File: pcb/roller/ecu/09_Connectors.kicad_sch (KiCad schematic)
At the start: 1 part, among them J5 6437288-3

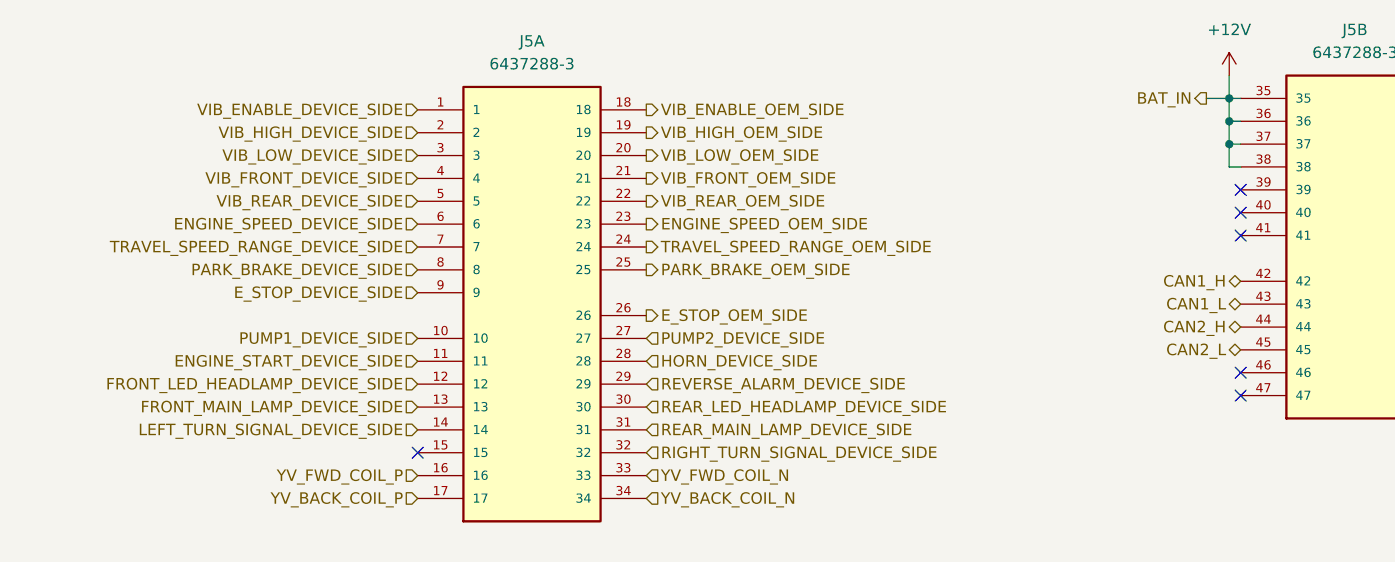
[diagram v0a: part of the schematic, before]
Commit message: Add design settings and DRC rules to ECU PCB configuration
- Introduced comprehensive design settings including defaults for various parameters such as line widths, text sizes, and pad dimensions.
- Added detailed DRC (Design Rule Check) exclusions and rule severities to enhance error handling and warnings during PCB design.
- Updated tuning pattern settings and teardrop parameters for improved track and pad connections.
- Cleared previously used designators for better organization and clarity in the design file.
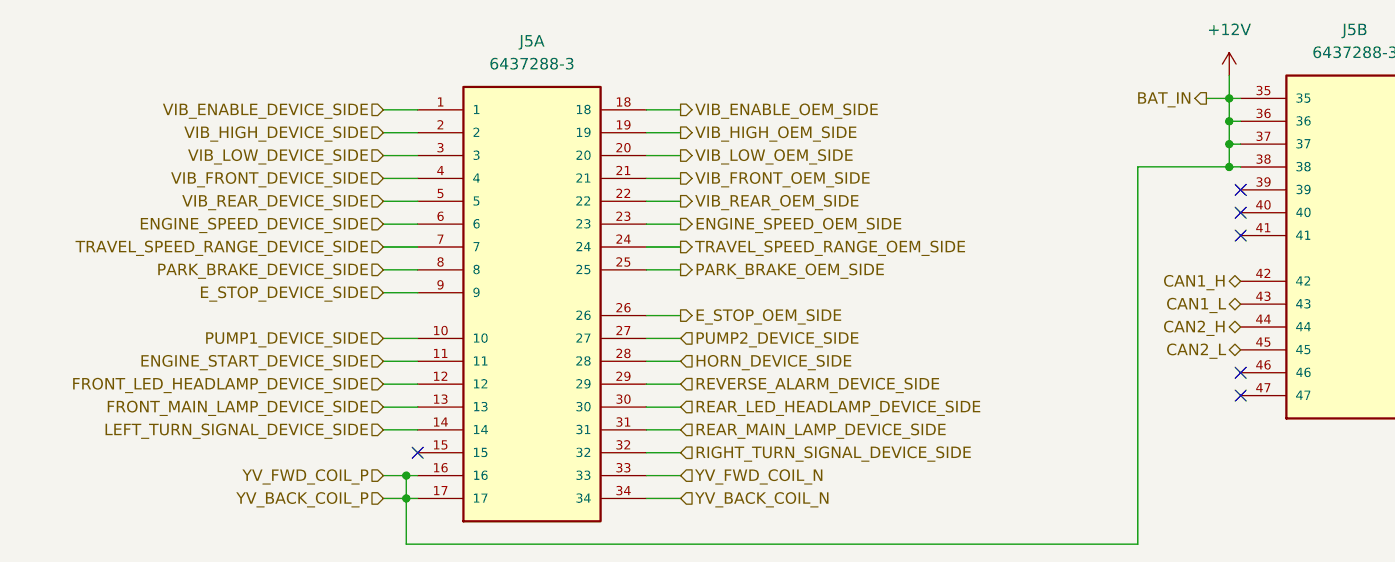
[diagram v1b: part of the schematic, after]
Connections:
- net YV_BACK_COIL_P is gone; now on net +12V: J5.17
- net YV_FWD_COIL_P is gone; now on net +12V: J5.16

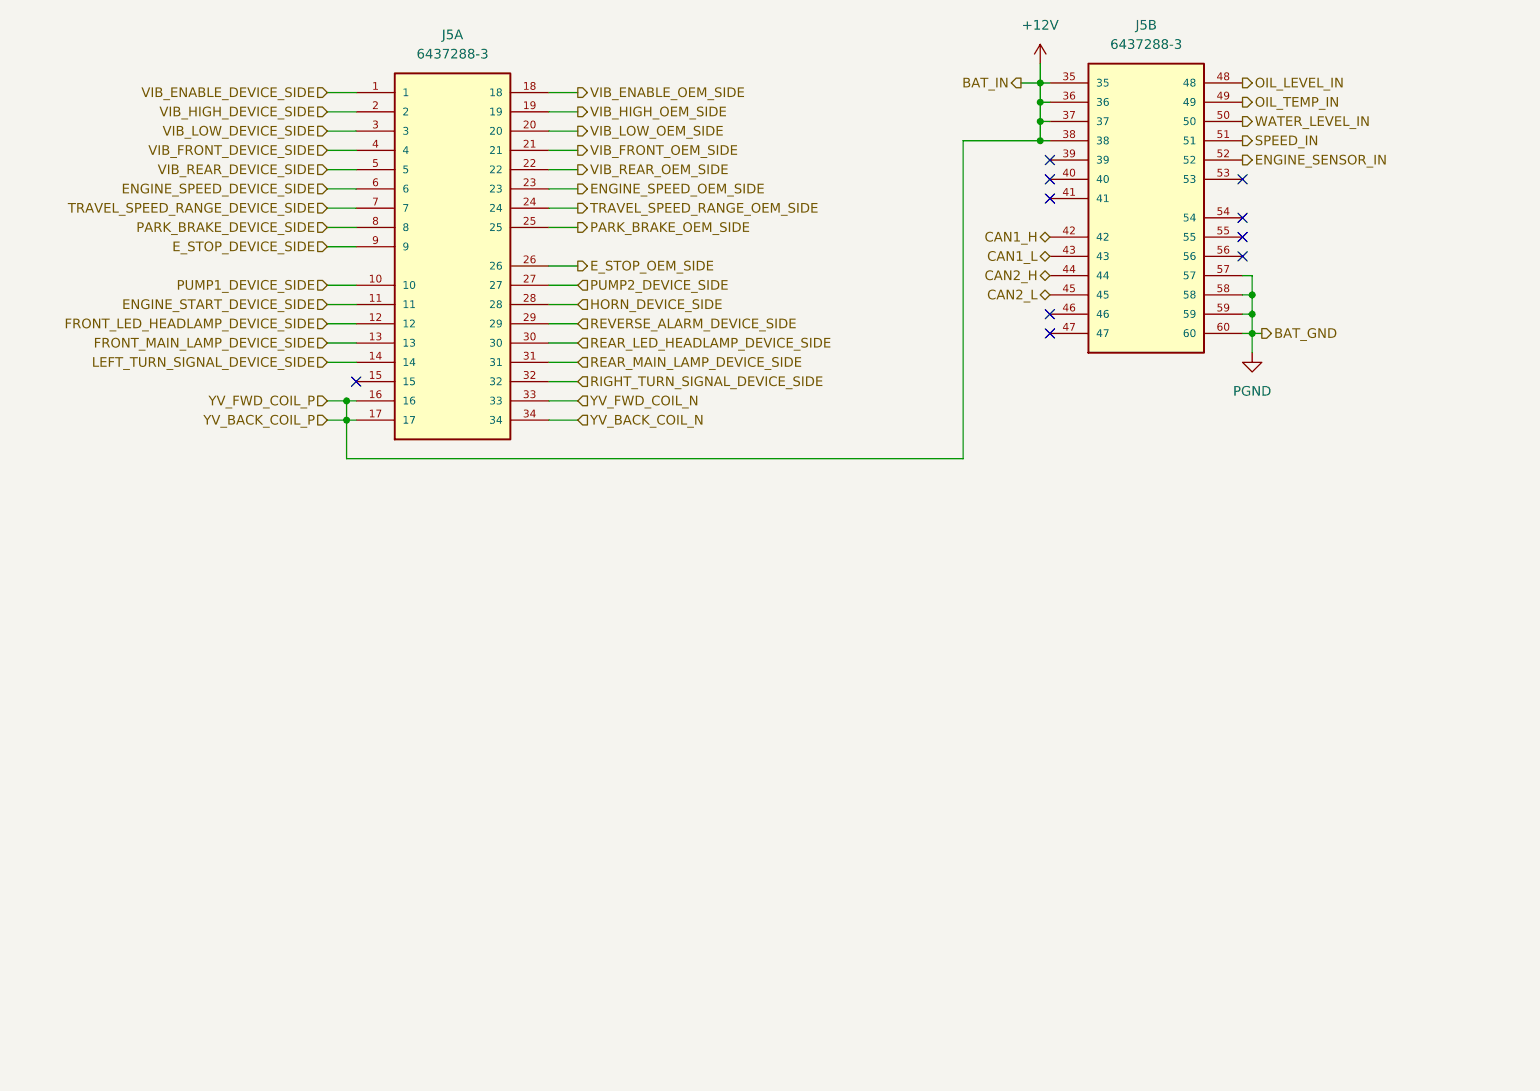
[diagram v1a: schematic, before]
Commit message: Add ESTOP_NC pin and wire connections in ECU schematic; update designators in PCB project
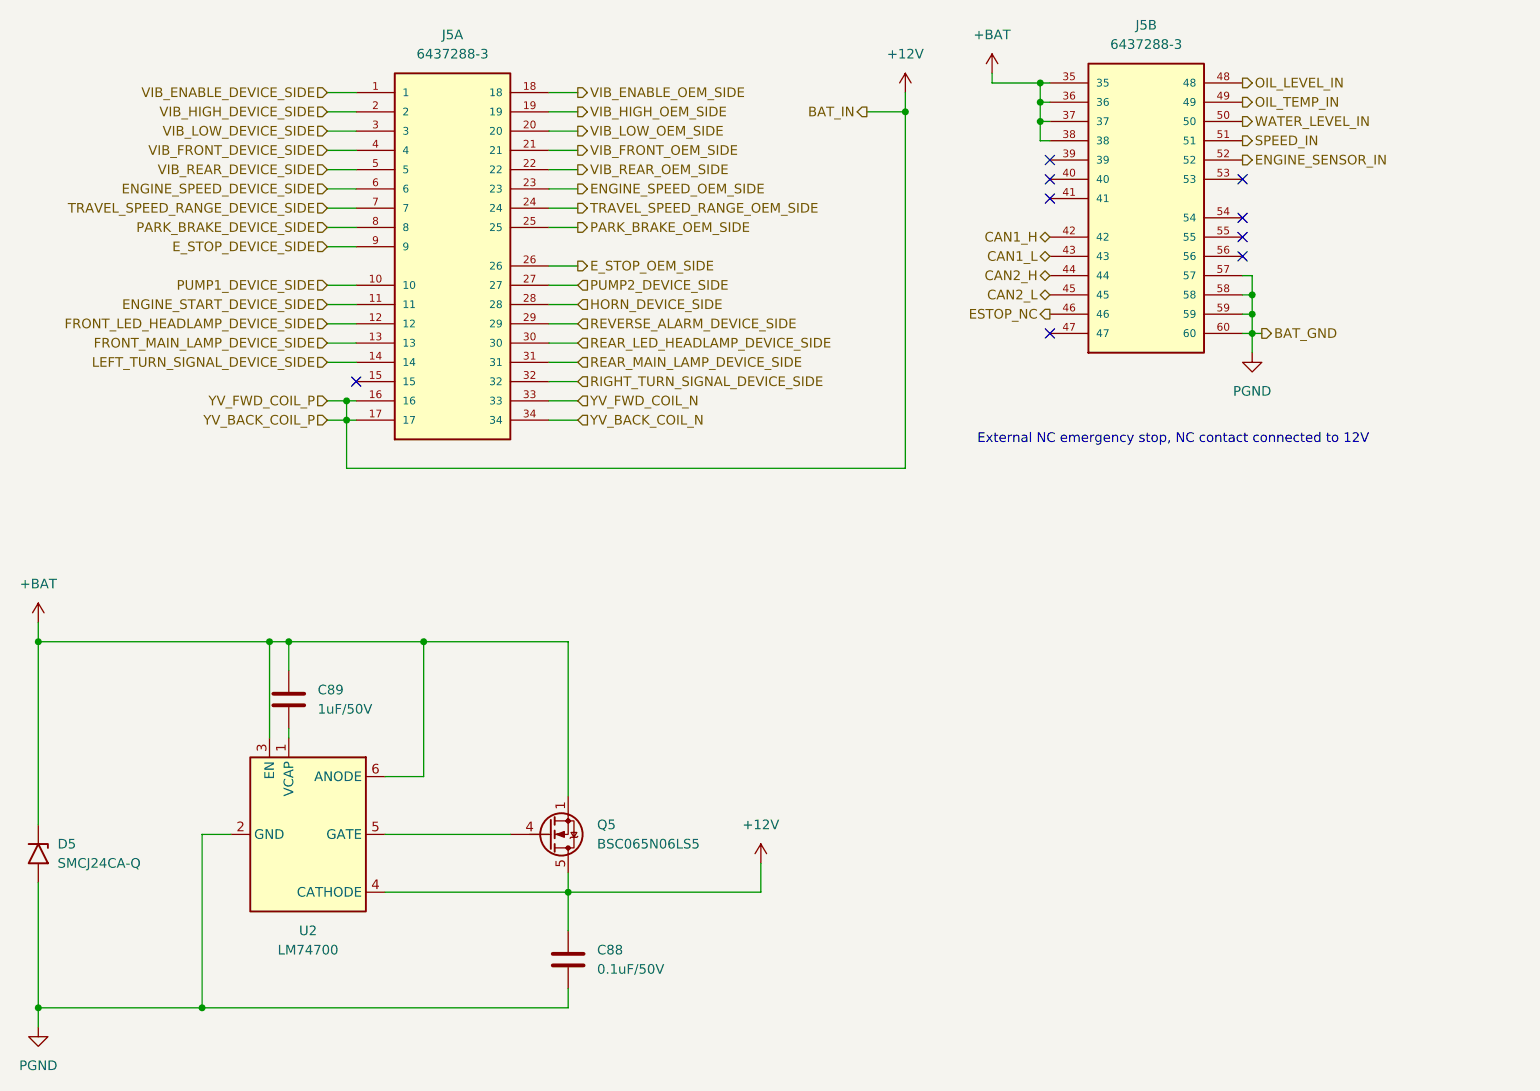
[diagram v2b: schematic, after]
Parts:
- added C88: 0.1uF/50V, Capacitor_SMD:C_0603_1608Metric, symbol Device:C
- added C89: 1uF/50V, Capacitor_SMD:C_0603_1608Metric, symbol Device:C
- added D5: SMCJ24CA-Q, Diode_SMD:D_SMC, symbol Diode:1.5SMCxxA
- added Q5: BSC065N06LS5, Package_TO_SOT_SMD:TDSON-8-1, symbol Transistor_FET:BSC060N10NS3G
- added U2: LM74700, Package_TO_SOT_SMD:SOT-23-6, symbol Power_Management:LM74700
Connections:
- net +12V: now also C88.1, Q5.5 (D), U2.4 (CATHODE); no longer J5.35, J5.36, J5.37, J5.38
- net PGND: now also C88.2, D5.2 (A2), U2.2 (GND)
- net ESTOP_NC: now reaches J5.46
- new net: C89.2, U2.1 (VCAP)
- new net: Q5.4 (G), U2.5 (GATE)
- new net +BAT: C89.1, D5.1 (A1), J5.35, J5.36, J5.37, J5.38, Q5.1 (S), Q5.2 (S), Q5.3 (S), U2.3 (EN), U2.6 (ANODE)
- no-connect marks 10 -> 9
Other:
- note added: "External NC emergency stop, NC contact connected to 12V"

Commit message: Refactor ECU schematic and project files
- Updated used designators in ecu.kicad_pro to reflect current components.
- Adjusted wire connections in ecu.kicad_sch for better layout and clarity.
- Added new wires and labels for ESTOP functionality.
- Modified pin placements and sizes for improved organization in the schematic.
- Ensured all changes maintain compatibility with existing design specifications.
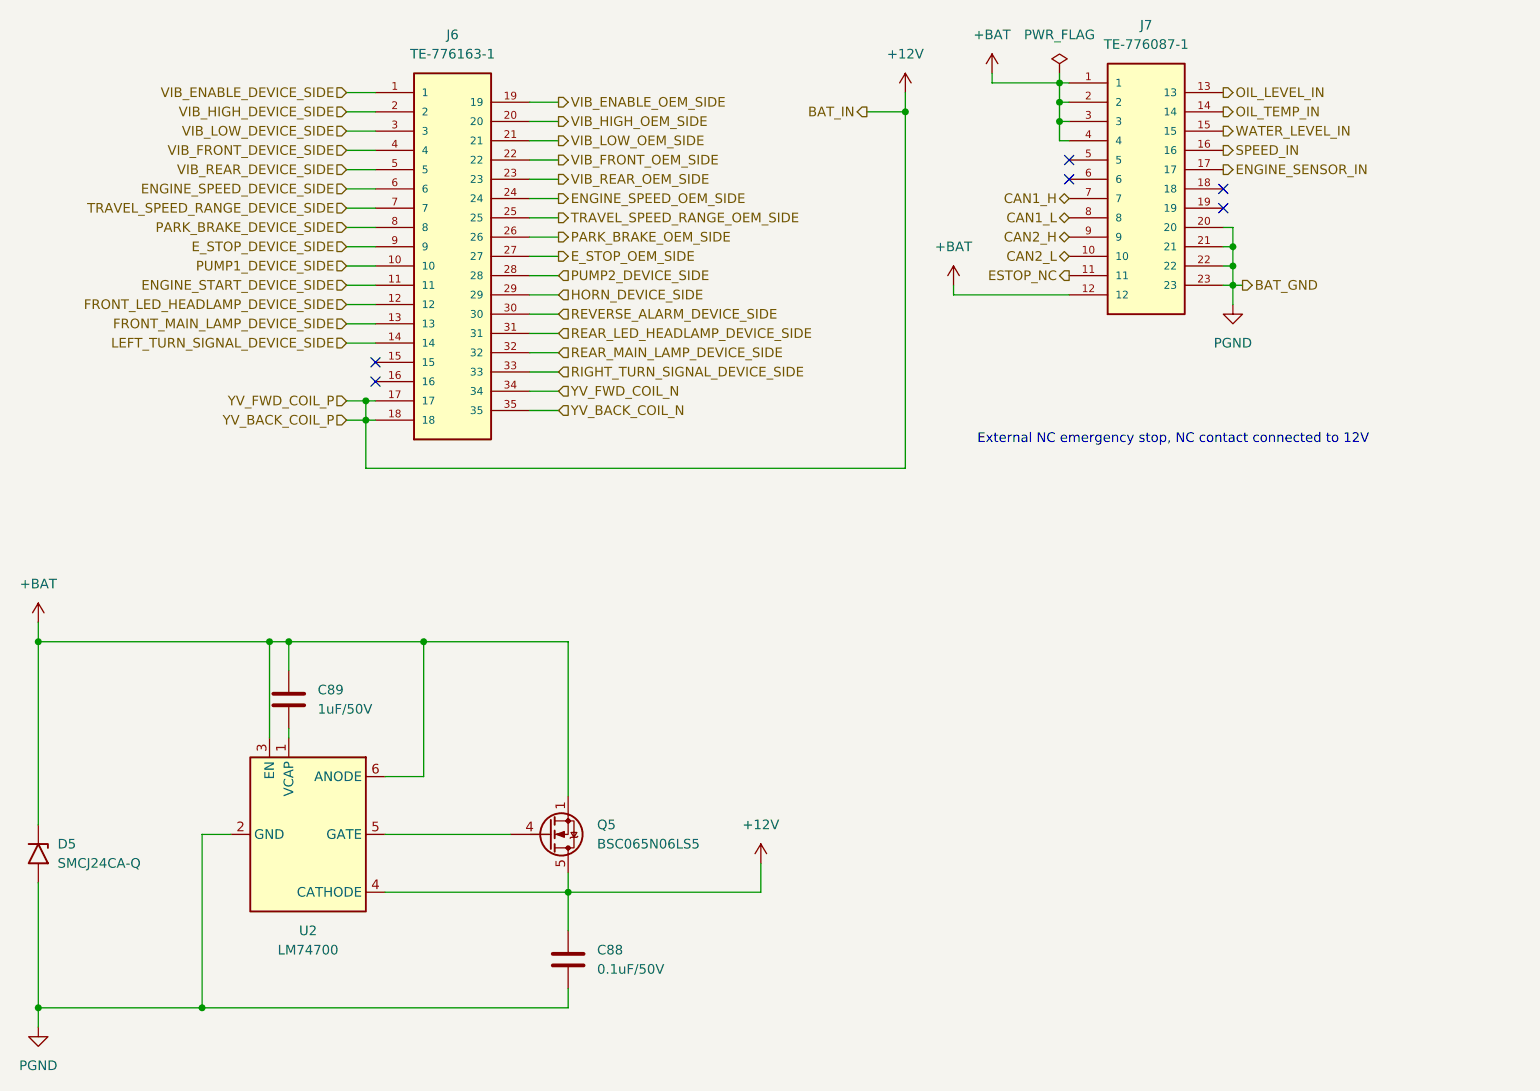
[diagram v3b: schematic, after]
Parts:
- removed J5: 6437288-3, Starlight:TE_6437288-3, symbol Starlight:6437288-3
- added J6: TE-776163-1, Starlight:TE_776163-1, symbol Starlight:TE-776163-1
- added J7: TE-776087-1, Starlight:TE_776087-1, symbol Starlight:TE-776087-1
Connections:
- net +12V: now also J6.17, J6.18
- net +BAT: now also J7.1, J7.12, J7.2, J7.3, J7.4
- net CAN1_H: now also J7.7
- net CAN1_L: now also J7.8
- net CAN2_H: now also J7.9
- net CAN2_L: now also J7.10
- net ENGINE_SENSOR_IN: now also J7.17
- net ENGINE_SPEED_DEVICE_SIDE: now also J6.6
- net ENGINE_SPEED_OEM_SIDE: now also J6.24
- net ENGINE_START_DEVICE_SIDE: now also J6.11
- net ESTOP_NC: now also J7.11
- net E_STOP_DEVICE_SIDE: now also J6.9
- net E_STOP_OEM_SIDE: now also J6.27
- net FRONT_LED_HEADLAMP_DEVICE_SIDE: now also J6.12
- net FRONT_MAIN_LAMP_DEVICE_SIDE: now also J6.13
- net HORN_DEVICE_SIDE: now also J6.29
- net LEFT_TURN_SIGNAL_DEVICE_SIDE: now also J6.14
- net OIL_LEVEL_IN: now also J7.13
- net OIL_TEMP_IN: now also J7.14
- net PARK_BRAKE_DEVICE_SIDE: now also J6.8
- net PARK_BRAKE_OEM_SIDE: now also J6.26
- net PGND: now also J7.20, J7.21, J7.22, J7.23
- net PUMP1_DEVICE_SIDE: now also J6.10
- net PUMP2_DEVICE_SIDE: now also J6.28
- net REAR_LED_HEADLAMP_DEVICE_SIDE: now also J6.31
- net REAR_MAIN_LAMP_DEVICE_SIDE: now also J6.32
- net REVERSE_ALARM_DEVICE_SIDE: now also J6.30
- net RIGHT_TURN_SIGNAL_DEVICE_SIDE: now also J6.33
- net SPEED_IN: now also J7.16
- net TRAVEL_SPEED_RANGE_DEVICE_SIDE: now also J6.7
- net TRAVEL_SPEED_RANGE_OEM_SIDE: now also J6.25
- net VIB_ENABLE_DEVICE_SIDE: now also J6.1
- net VIB_ENABLE_OEM_SIDE: now also J6.19
- net VIB_FRONT_DEVICE_SIDE: now also J6.4
- net VIB_FRONT_OEM_SIDE: now also J6.22
- net VIB_HIGH_DEVICE_SIDE: now also J6.2
- net VIB_HIGH_OEM_SIDE: now also J6.20
- net VIB_LOW_DEVICE_SIDE: now also J6.3
- net VIB_LOW_OEM_SIDE: now also J6.21
- net VIB_REAR_DEVICE_SIDE: now also J6.5
- net VIB_REAR_OEM_SIDE: now also J6.23
- net WATER_LEVEL_IN: now also J7.15
- net YV_BACK_COIL_N: now also J6.35
- net YV_FWD_COIL_N: now also J6.34
- no-connect marks 9 -> 6

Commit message: Implement code changes to enhance functionality and improve performance
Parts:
- added H1, H2, H3, H4: MountingHole_Pad, MountingHole:MountingHole_3.2mm_M3_ISO7380_Pad, symbol Mechanical:MountingHole_Pad
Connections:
- new net GND: H1.1, H2.1, H3.1, H4.1

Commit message: fix: update power symbol and reference designators in ECU schematic and PCB files
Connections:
- net +12V: now also J7.12
- net +BAT: no longer J7.12
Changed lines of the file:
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@@
+	)
+	(symbol
+		(lib_id "power:+12V")
+		(at 158.75 78.74 0)
+		(unit 1)
+		(body_style 1)
+		(exclude_from_sim no)
+		(in_bom yes)
+		(on_board yes)
+		(in_pos_files yes)
+		(dnp no)
+		(fields_autoplaced yes)
+		(property "Reference" "#PWR0129"
+			(at 158.75 82.55 0)
+			(hide yes)
+			(show_name no)
+			(do_not_autoplace no)
+			(effects
+				(font
+					(size 1.27 1.27)
+				)
+			)
+		)
+		(property "Value" "+12V"
+			(at 158.75 73.66 0)
+			(show_name no)
+			(do_not_autoplace no)
+			(effects
+				(font
+					(size 1.27 1.27)
+				)
+			)
+		)
+		(property "Footprint" ""
+			(at 158.75 78.74 0)
+			(hide yes)
+			(show_name no)
+			(do_not_autoplace no)
+			(effects
+				(font
+					(size 1.27 1.27)
+				)
+			)
+		)
+		(property "Datasheet" ""
+			(at 158.75 78.74 0)
+			(hide yes)
+			(show_name no)
+			(do_not_autoplace no)
+			(effects
+				(font
+					(size 1.27 1.27)
+				)
+			)
+		)
+		(property "Description" "Power symbol creates a global label with name \"+12V\""
+			(at 158.75 78.74 0)
+			(hide yes)
+			(show_name no)
+			(do_not_autoplace no)
+			(effects
+				(font
+					(size 1.27 1.27)
+				)
+			)
+		)
+		(pin "1"
+		)
+		(instances
+			(project "ecu"
+				(path "/e5f3c8f3-31b1-4864-b028-38bb5e50c369/70e522b8-5e86-4012-974f-127d60591632"
+					(reference "#PWR0129")
+					(unit 1)
+				)
+			)
+		)
 	)
 	(symbol
@@
 					(unit 1)
 				)
-			)
-		)
-	)
-	(symbol
-		(lib_id "power:+BATT")
-		(at 158.75 78.74 0)
-		(unit 1)
-		(body_style 1)
-		(exclude_from_sim no)
-		(in_bom yes)
-		(on_board yes)
-		(in_pos_files yes)
-		(dnp no)
-		(fields_autoplaced yes)
-		(property "Reference" "#PWR0129"
-			(at 158.75 82.55 0)
-			(hide yes)
-			(show_name no)
-			(do_not_autoplace no)
-			(effects
-				(font
-					(size 1.27 1.27)
-				)
-			)
-		)
-		(property "Value" "+BAT"
-			(at 158.75 73.66 0)
-			(show_name no)
-			(do_not_autoplace no)
-			(effects
-				(font
-					(size 1.27 1.27)
-				)
-			)
-		)
-		(property "Footprint" ""
-			(at 158.75 78.74 0)
-			(hide yes)
-			(show_name no)
-			(do_not_autoplace no)
-			(effects
-				(font
-					(size 1.27 1.27)
-				)
-			)
-		)
-		(property "Datasheet" ""
-			(at 158.75 78.74 0)
-			(hide yes)
-			(show_name no)
-			(do_not_autoplace no)
-			(effects
-				(font
-					(size 1.27 1.27)
-				)
-			)
-		)
-		(property "Description" "Power symbol creates a global label with name \"+BATT\""
-			(at 158.75 78.74 0)
-			(hide yes)
-			(show_name no)
-			(do_not_autoplace no)
-			(effects
-				(font
-					(size 1.27 1.27)
-				)
-			)
-		)
-		(pin "1"
-		)
-		(instances
-			(project "ecu"
-				(path "/e5f3c8f3-31b1-4864-b028-38bb5e50c369/70e522b8-5e86-4012-974f-127d60591632"
-					(reference "#PWR0129")
-					(unit 1)
-				)
